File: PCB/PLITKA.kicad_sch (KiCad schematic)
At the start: 47 parts, among them SW1 SW_DPDT_x2, SW10 MX_SW_HS, SW11 MX_SW_HS, SW12 MX_SW_HS, SW13 MX_SW_HS, SW14 MX_SW_HS, SW15 MX_SW_HS, SW16 MX_SW_HS, SW17 MX_SW_HS, SW18 MX_SW_HS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

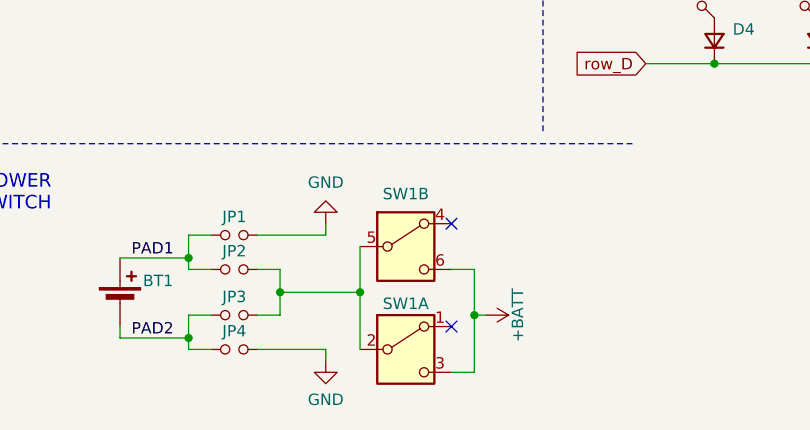
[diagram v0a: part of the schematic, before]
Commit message: Fix: replace SW1 DPDT symbol with SPDT to match the footprint
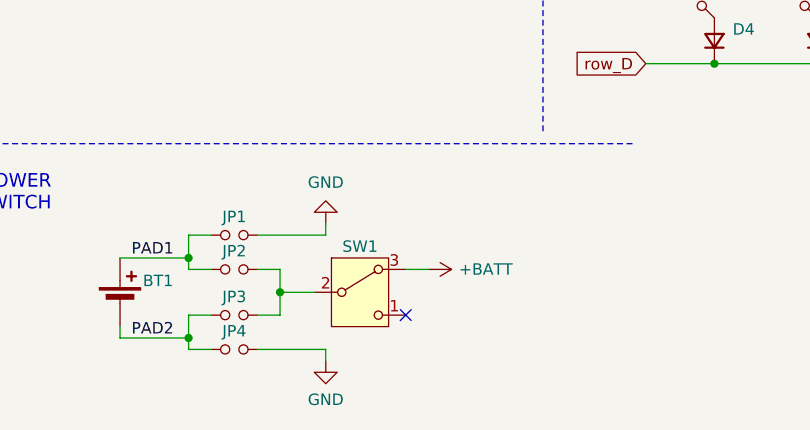
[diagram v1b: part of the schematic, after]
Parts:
- removed SW1: SW_DPDT_x2, symbol Switch:SW_DPDT_x2
- added SW1: SW_SPDT_321, PLITKA:MSK12C02_reversible, symbol Switch:SW_SPDT_321
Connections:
- net +BATT: now also SW1.3 (A)
- net at JP2.2, JP3.2: now also SW1.2 (B)
- no-connect marks 14 -> 13
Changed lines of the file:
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@@
 	)
 	(junction
-		(at 72.39 123.19)
-		(diameter 0)
-		(color 0 0 0 0)
-	)
-	(junction
 		(at 110.49 77.47)
 		(diameter 0)
@@
 	)
 	(junction
-		(at 50.8 120.65)
-		(diameter 0)
-		(color 0 0 0 0)
-	)
-	(junction
 		(at 116.84 48.26)
 		(diameter 0)
@@
 	)
 	(junction
-		(at 59.69 120.65)
-		(diameter 0)
-		(color 0 0 0 0)
-	)
-	(junction
 		(at 116.84 30.48)
 		(diameter 0)
@@
 	)
 	(junction
+		(at 50.8 120.65)
+		(diameter 0)
+		(color 0 0 0 0)
+	)
+	(junction
 		(at 93.98 48.26)
 		(diameter 0)
@@
 	)
 	(no_connect
-		(at 69.85 124.46)
+		(at 64.77 123.19)
 	)
 	(no_connect
@@
 	)
 	(no_connect
-		(at 69.85 113.03)
-	)
-	(no_connect
 		(at 24.13 45.72)
 	)
@@
 	(wire
 		(pts
-			(xy 72.39 118.11) (xy 69.85 118.11)
-		)
-		(stroke
-			(width 0)
-			(type default)
-		)
-	)
-	(wire
-		(pts
 			(xy 40.64 118.11) (xy 43.18 118.11)
 		)
@@
 	(wire
 		(pts
-			(xy 59.69 120.65) (xy 59.69 127)
-		)
-		(stroke
-			(width 0)
-			(type default)
-		)
-	)
-	(wire
-		(pts
 			(xy 93.98 24.13) (xy 93.98 30.48)
 		)
@@
 	(wire
 		(pts
-			(xy 105.41 67.31) (xy 105.41 85.09)
+			(xy 67.31 118.11) (xy 64.77 118.11)
 		)
 		(stroke
@@
 	(wire
 		(pts
-			(xy 48.26 123.19) (xy 50.8 123.19)
+			(xy 105.41 67.31) (xy 105.41 85.09)
 		)
 		(stroke
@@
 	(wire
 		(pts
-			(xy 40.64 125.73) (xy 40.64 123.19)
+			(xy 48.26 123.19) (xy 50.8 123.19)
 		)
 		(stroke
@@
 	(wire
 		(pts
-			(xy 72.39 129.54) (xy 69.85 129.54)
+			(xy 40.64 125.73) (xy 40.64 123.19)
 		)
 		(stroke
@@
 	(wire
 		(pts
-			(xy 50.8 120.65) (xy 59.69 120.65)
+			(xy 50.8 120.65) (xy 54.61 120.65)
 		)
 		(stroke
@@
 	(wire
 		(pts
-			(xy 72.39 123.19) (xy 72.39 118.11)
-		)
-		(stroke
-			(width 0)
-			(type default)
-		)
-	)
-	(wire
-		(pts
 			(xy 127 30.48) (xy 127 48.26)
 		)
@@
 	(wire
 		(pts
-			(xy 72.39 123.19) (xy 72.39 129.54)
-		)
-		(stroke
-			(width 0)
-			(type default)
-		)
-	)
-	(wire
-		(pts
 			(xy 55.88 114.3) (xy 55.88 113.03)
 		)
@@
 	(wire
 		(pts
-			(xy 59.69 115.57) (xy 59.69 120.65)
-		)
-		(stroke
-			(width 0)
-			(type default)
-		)
-	)
-	(wire
-		(pts
 			(xy 132.08 58.42) (xy 143.51 58.42)
 		)
@@
 	(wire
 		(pts
-			(xy 73.66 123.19) (xy 72.39 123.19)
-		)
-		(stroke
-			(width 0)
-			(type default)
-		)
-	)
-	(wire
-		(pts
 			(xy 132.08 77.47) (xy 143.51 77.47)
 		)
@@
 	(symbol
 		(lib_id "power:+BATT")
-		(at 73.66 123.19 270)
+		(at 67.31 118.11 270)
 		(unit 1)
 		(body_style 1)
@@
 		(dnp no)
 		(property "Reference" "#PWR6"
-			(at 69.85 123.19 0)
+			(at 63.5 118.11 0)
 			(hide yes)
 			(show_name no)
@@
 		)
 		(property "Value" "+BATT"
-			(at 77.216 123.19 0)
+			(at 73.66 118.11 90)
 			(show_name no)
 			(do_not_autoplace no)
@@
 		)
 		(property "Footprint" ""
-			(at 73.66 123.19 0)
+			(at 67.31 118.11 0)
 			(hide yes)
 			(show_name no)
@@
 		)
 		(property "Datasheet" ""
-			(at 73.66 123.19 0)
+			(at 67.31 118.11 0)
 			(hide yes)
 			(show_name no)
@@
 		)
 		(property "Description" "Power symbol creates a global label with name \"+BATT\""
-			(at 73.66 123.19 0)
+			(at 67.31 118.11 0)
 			(hide yes)
 			(show_name no)
@@
 	)
 	(symbol
+		(lib_id "Switch:SW_SPDT_321")
+		(at 59.69 120.65 0)
+		(unit 1)
+		(body_style 1)
+		(exclude_from_sim no)
+		(in_bom yes)
+		(on_board yes)
+		(in_pos_files yes)
+		(dnp no)
+		(property "Reference" "SW1"
+			(at 59.69 115.57 0)
+			(show_name no)
+			(do_not_autoplace no)
+			(effects
+				(font
+					(size 1.27 1.27)
+				)
+			)
+		)
+		(property "Value" "SW_SPDT_321"
+			(at 59.69 125.73 0)
+			(hide yes)
+			(show_name no)
+			(do_not_autoplace no)
+			(effects
+				(font
+					(size 1.27 1.27)
+				)
+			)
+		)
+		(property "Footprint" "PLITKA:MSK12C02_reversible"
+			(at 59.69 120.65 0)
+			(hide yes)
+			(show_name no)
+			(do_not_autoplace no)
+			(effects
+				(font
+					(size 1.27 1.27)
+				)
+			)
+		)
+		(property "Datasheet" ""
+			(at 59.69 120.65 0)
+			(hide yes)
+			(show_name no)
+			(do_not_autoplace no)
+			(effects
+				(font
+					(size 1.27 1.27)
+				)
+			)
+		)
+		(property "Description" "Switch, single pole double throw"
+			(at 59.69 120.65 0)
+			(hide yes)
+			(show_name no)
+			(do_not_autoplace no)
+			(effects
+				(font
+					(size 1.27 1.27)
+				)
+			)
+		)
+		(pin "1"
+		)
+		(pin "2"
+		)
+		(pin "3"
+		)
+		(instances
+			(project "PLITKA"
+				(path "/231ead31-262f-44fe-a25c-f58d2465dcca"
+					(reference "SW1")
+					(unit 1)
+				)
+			)
+		)
+	)
+	(symbol
 		(lib_id "PLITKA:MX_SW_HS")
 		(at 119.38 33.02 0)
@@
 					(unit 1)
 				)
-			)
-		)
-	)
-	(symbol
-		(lib_id "Switch:SW_DPDT_x2")
-		(at 64.77 115.57 0)
-		(unit 2)
-		(body_style 1)
-		(exclude_from_sim no)
-		(in_bom yes)
-		(on_board yes)
-		(in_pos_files yes)
-		(dnp no)
-		(property "Reference" "SW1"
-			(at 64.77 109.728 0)
-			(show_name no)
-			(do_not_autoplace no)
-			(effects
-				(font
-					(size 1.27 1.27)
-				)
-			)
-		)
-		(property "Value" "SW_DPDT_x2"
-			(at 64.77 109.22 0)
-			(hide yes)
-			(show_name no)
-			(do_not_autoplace no)
-			(effects
-				(font
-					(size 1.27 1.27)
-				)
-			)
-		)
-		(property "Footprint" ""
-			(at 64.77 115.57 0)
-			(hide yes)
-			(show_name no)
-			(do_not_autoplace no)
-			(effects
-				(font
-					(size 1.27 1.27)
-				)
-			)
-		)
-		(property "Datasheet" ""
-			(at 64.77 115.57 0)
-			(hide yes)
-			(show_name no)
-			(do_not_autoplace no)
-			(effects
-				(font
-					(size 1.27 1.27)
-				)
-			)
-		)
-		(property "Description" "Switch, dual pole double throw, separate symbols"
-			(at 64.77 115.57 0)
-			(hide yes)
-			(show_name no)
-			(do_not_autoplace no)
-			(effects
-				(font
-					(size 1.27 1.27)
-				)
-			)
-		)
-		(pin "1"
-		)
-		(pin "2"
-		)
-		(pin "3"
-		)
-		(pin "4"
-		)
-		(pin "5"
-		)
-		(pin "6"
-		)
-		(instances
-			(project "PLITKA"
-				(path "/231ead31-262f-44fe-a25c-f58d2465dcca"
-					(reference "SW1")
-					(unit 2)
-				)
-			)
-		)
-	)
-	(symbol
-		(lib_id "Switch:SW_DPDT_x2")
-		(at 64.77 127 0)
-		(unit 1)
-		(body_style 1)
-		(exclude_from_sim no)
-		(in_bom yes)
-		(on_board yes)
-		(in_pos_files yes)
-		(dnp no)
-		(property "Reference" "SW1"
-			(at 64.77 121.92 0)
-			(show_name no)
-			(do_not_autoplace no)
-			(effects
-				(font
-					(size 1.27 1.27)
-				)
-			)
-		)
-		(property "Value" "SW_DPDT_x2"
-			(at 64.77 132.08 0)
-			(hide yes)
-			(show_name no)
-			(do_not_autoplace no)
-			(effects
-				(font
-					(size 1.27 1.27)
-				)
-			)
-		)
-		(property "Footprint" ""
-			(at 64.77 127 0)
-			(hide yes)
-			(show_name no)
-			(do_not_autoplace no)
-			(effects
-				(font
-					(size 1.27 1.27)
-				)
-			)
-		)
-		(property "Datasheet" ""
-			(at 64.77 127 0)
-			(hide yes)
-			(show_name no)
-			(do_not_autoplace no)
-			(effects
-				(font
-					(size 1.27 1.27)
-				)
-			)
-		)
-		(property "Description" "Switch, dual pole double throw, separate symbols"
-			(at 64.77 127 0)
-			(hide yes)
-			(show_name no)
-			(do_not_autoplace no)
-			(effects
-				(font
-					(size 1.27 1.27)
-				)
-			)
-		)
-		(pin "1"
-		)
-		(pin "2"
-		)
-		(pin "3"
-		)
-		(pin "4"
-		)
-		(pin "5"
-		)
-		(pin "6"
-		)
-		(instances
-			(project "PLITKA"
-				(path "/231ead31-262f-44fe-a25c-f58d2465dcca"
-					(reference "SW1")
-					(unit 1)
-				)
